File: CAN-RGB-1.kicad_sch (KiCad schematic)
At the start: 9 parts, among them P1 USB_C_Plug_USB2.0, U1 MCP2551-I_SN, U2 ATmega32U4-A, Y1 16MHz

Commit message: reset and labels added
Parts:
- added C3: 0.1 uF, symbol Device:C
- added R4: 10 K, symbol Device:R
- added R5: 1 K, symbol Device:R
- added SW1: SW_Push, symbol Switch:SW_Push
- R3: value 10k -> 10 K
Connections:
- net +5V: now also R4.1
- net GND: now also C3.2, SW1.1
- net UGND: now reaches P1.A1 (GND), P1.A12 (GND), P1.B1 (GND), P1.B12 (GND), U2.5 (UGND)
- net RST: now reaches U2.13 (~{RESET})
- net RST: now also C3.1, R4.2, R5.2
- net RX: now reaches U1.4 (RXD), U2.20 (PD2)
- net TX: now reaches U1.1 (TXD), U2.21 (PD3)
- net CANL: now reaches U1.6 (CANL)
- net CANH: now reaches U1.7 (CANH)
- new net: R5.1, SW1.2
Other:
- moved on the sheet: Y1

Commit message: schematic almost finished. 2551->61,pins and power supply
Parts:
- removed R3: 10 K, symbol Device:R
- removed U1: MCP2551-I_SN, MCP2551-I_SN:SOIC127P599X175-8N, symbol MCP2551-I_SN:MCP2551-I_SN
- added C4: .1 uF, symbol Device:C
- added C5: 4700 pF, symbol Device:C
- added C6, C7: 10 uF, symbol Device:C
- added J1: Conn_01x06_Socket, symbol Connector:Conn_01x06_Socket
- added J2: Conn_01x03_Socket, symbol Connector:Conn_01x03_Socket
- added L1: 5.6 uH, symbol Device:L
- added PS1: TSR_1-2450SM, TSR_1-2450SM:CONV_TSR_1-2450SM, symbol TSR_1-2450SM:TSR_1-2450SM
- added R6, R7: 60, symbol Device:R
- added R8: 300, symbol Device:R
- added U3: MCP2561-E_SN, MCP2561-E_SN:SOIC127P600X175-8N, symbol MCP2561-E_SN:MCP2561-E_SN
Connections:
- net +5V: now also C4.1, PS1.5 (+VOUT), U3.3 (VDD)
- net CANH: now also J1.2 (Pin_2), J1.3 (Pin_3), R6.1, U3.7 (CANH)
- net CANL: now also J1.4 (Pin_4), J1.5 (Pin_5), R7.2, U3.6 (CANL)
- net DIO: now also J2.2 (Pin_2)
- net GND: now also C4.2, C5.2, C6.2, C7.2, J1.6 (Pin_6), J2.3 (Pin_3), PS1.7 (GND), PS1.9 (GND), U3.2 (VSS)
- net RX: now also U3.4 (RXD)
- net TX: now also U3.1 (TXD)
- new net: C6.1, J2.1 (Pin_1), L1.2, PS1.1 (+VIN)
- new net: C5.1, R6.2, R7.1, R8.2
- new net: PS1.10 (NC), PS1.6 (NC)
- new net +12V: C7.1, J1.1 (Pin_1), L1.1
- new net SPLIT: R8.1, U3.5 (SPLIT)
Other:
- moved on the sheet: C1, C2, C3, P1, R1, R2, R4, R5, SW1, U2, Y1

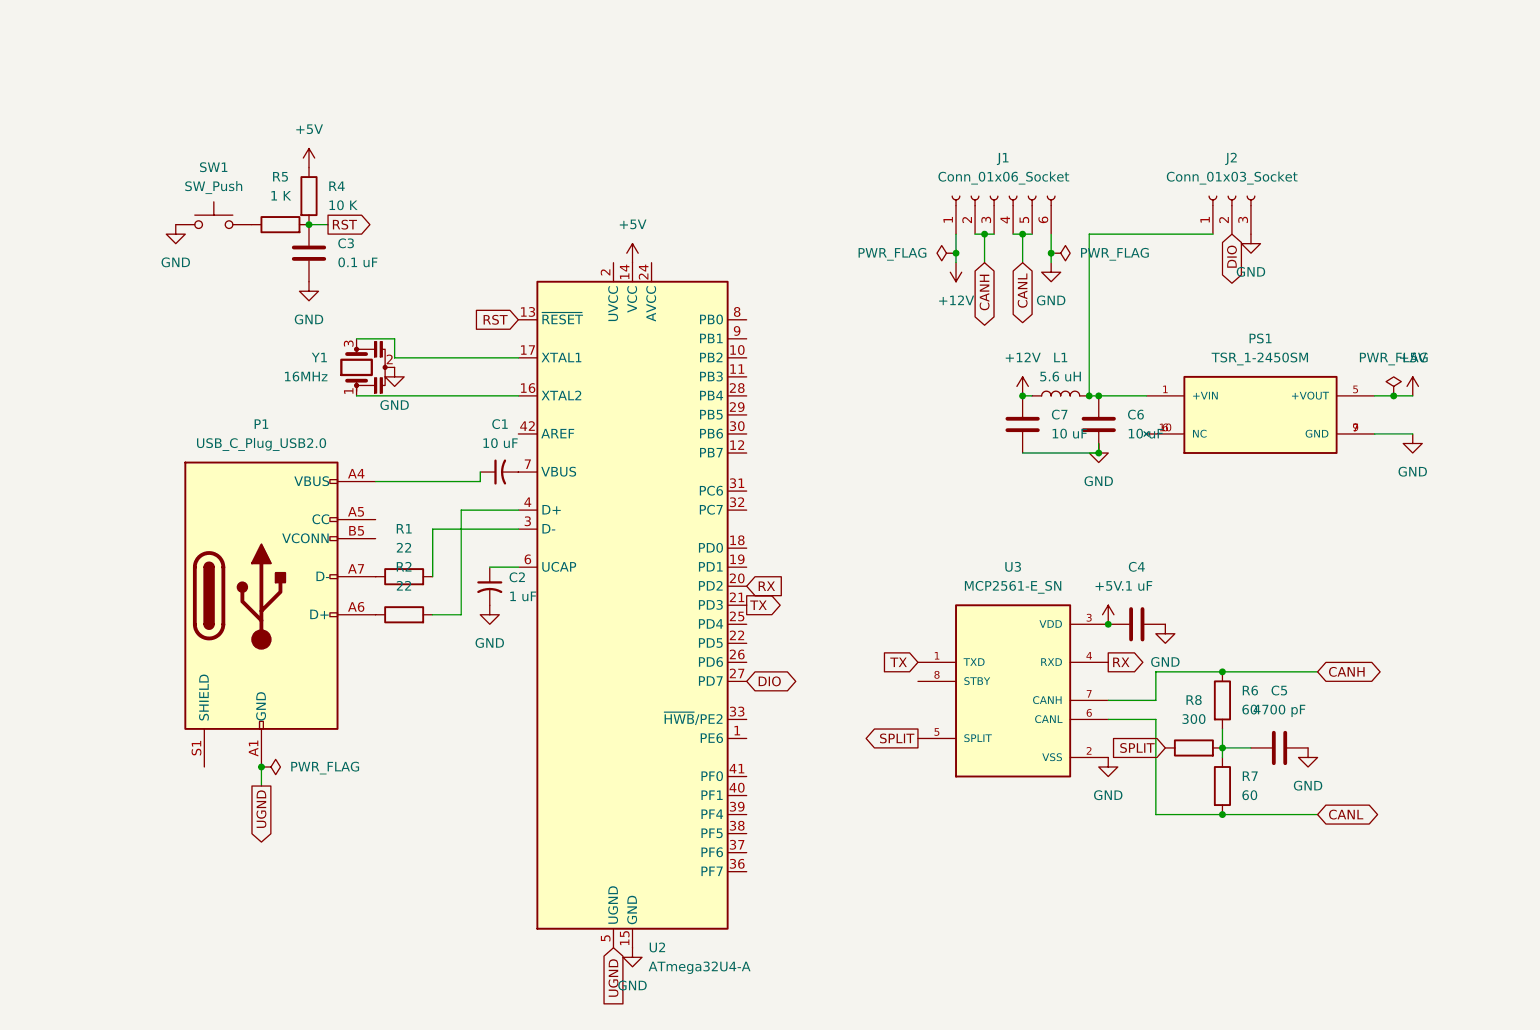
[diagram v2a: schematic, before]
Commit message: more footprints added, schematic needs review
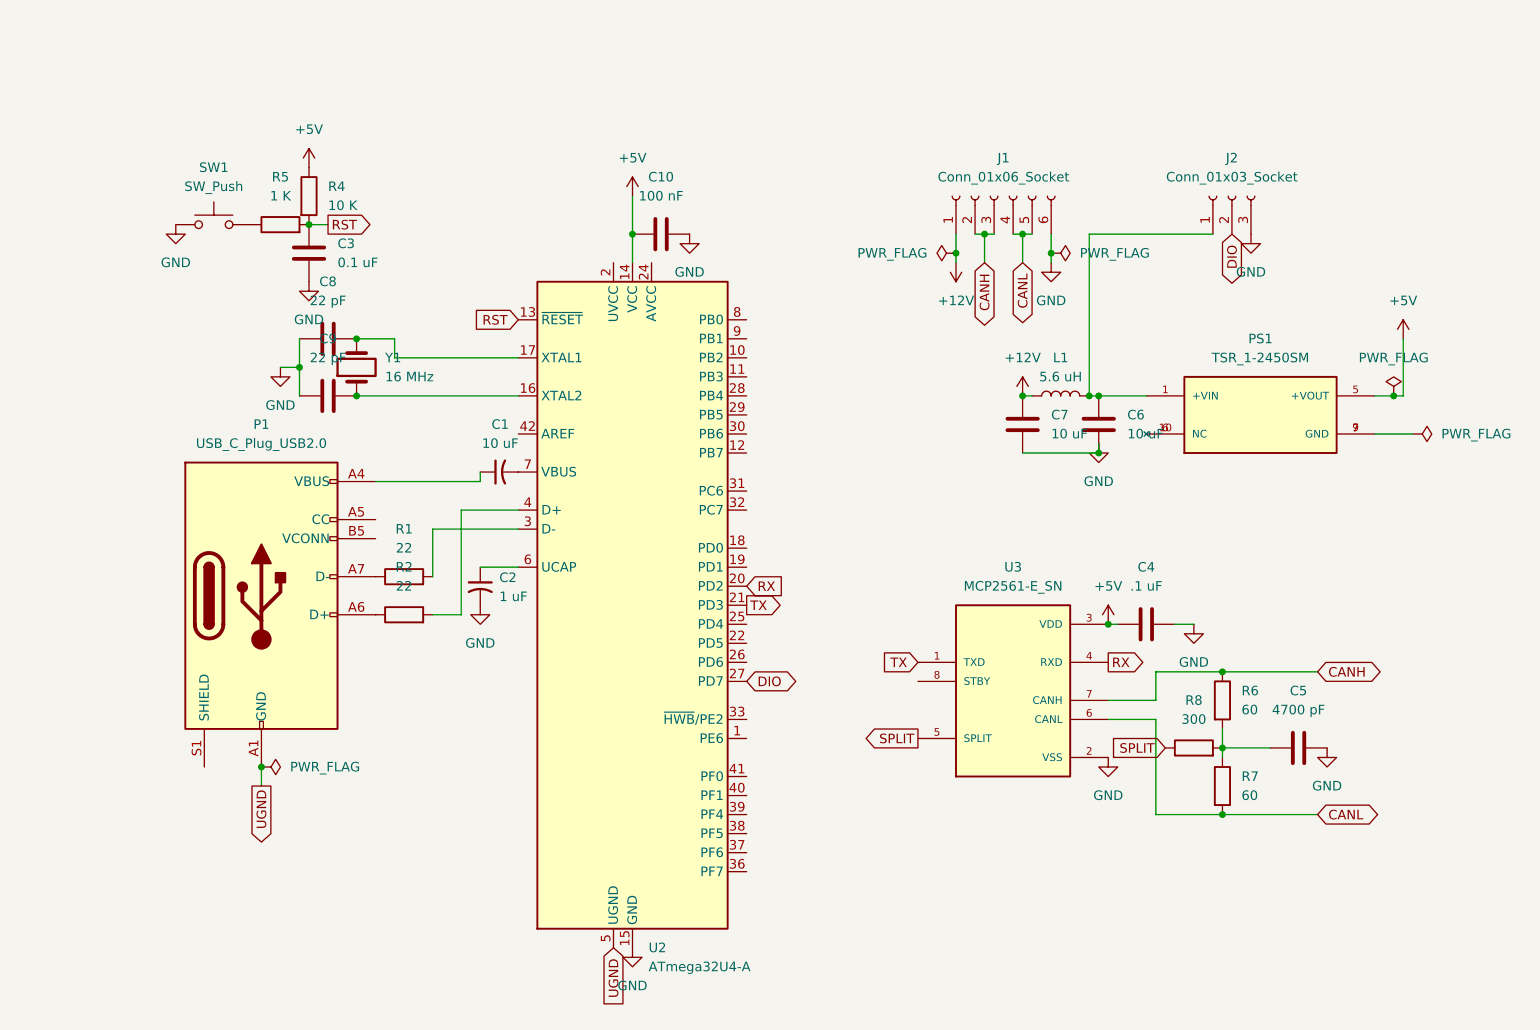
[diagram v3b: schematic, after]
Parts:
- removed Y1: 16MHz, symbol Device:Resonator
- added C10: 100 nF, Capacitor_SMD:C_0201_0603Metric, symbol Device:C
- added C8, C9: 22 pF, Capacitor_SMD:C_0201_0603Metric, symbol Device:C
- added Y1: 16 MHz, Crystal:Crystal_HC49-U_Vertical, symbol Device:Crystal
- C1, C2, C3, C4, C5, C6, C7: footprint (none) -> Capacitor_SMD:C_0201_0603Metric
- J1: footprint (none) -> Connector_Wire:SolderWire-0.1sqmm_1x06_P3.6mm_D0.4mm_OD1mm
- J2: footprint (none) -> Connector_Wire:SolderWire-0.1sqmm_1x03_P3.6mm_D0.4mm_OD1mm
- L1: footprint (none) -> Inductor_SMD:L_0201_0603Metric
- R1, R2: footprint (none) -> Resistor_SMD:R_0402_1005Metric
- R4: footprint (none) -> Resistor_SMD:R_0612_1632Metric
- R5, R6, R7, R8: footprint (none) -> Resistor_SMD:R_0201_0603Metric
- SW1: footprint (none) -> Button_Switch_SMD:SW_SPST_CK_RS282G05A3
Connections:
- net +5V: now also C10.1
- net GND: now also C10.2, C8.1, C9.1; no longer PS1.7 (GND), PS1.9 (GND)
- net at U2.16 (XTAL2): now also C9.2, Y1.1
- net at U2.17 (XTAL1): now also C8.2, Y1.2
- new net: PS1.7 (GND), PS1.9 (GND)
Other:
- moved on the sheet: C2, C4, C5

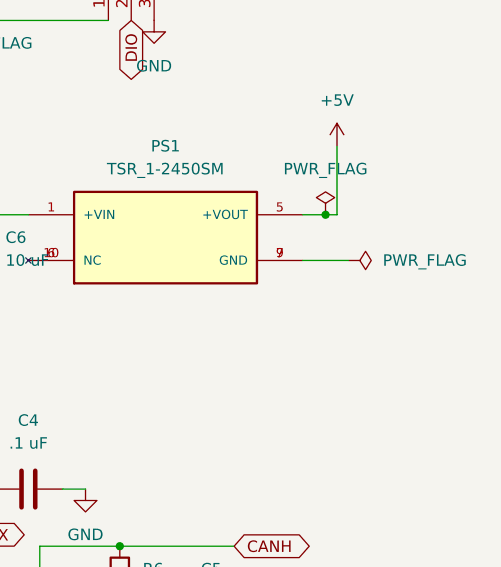
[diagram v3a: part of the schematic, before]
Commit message: Beginnings of PCB layout, needs to be reviewed, organized, and finalized.
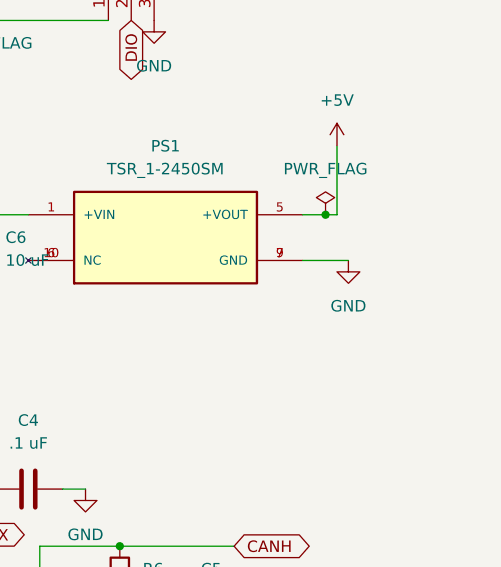
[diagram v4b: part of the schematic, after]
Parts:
- P1: footprint (none) -> Connector_USB:USB_C_Receptacle_HCTL_HC-TYPE-C-16P-01A
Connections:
- net GND: now also PS1.7 (GND), PS1.9 (GND)
